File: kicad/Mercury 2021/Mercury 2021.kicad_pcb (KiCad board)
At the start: 2 copper layers, 100 x 100 mm, 46 parts, among them J1 Batt_Power, J10 3.3v rail, J13 Screw_Terminal_01x02, J14 Screw_Terminal_01x02, J15 Raspberry_Pi_2_3, J16 Sensors_Extra, J17 Arduino_Extra_Power, J18 Arduino_Extra_Comm, J19 Arduino_Extra_Digital, J2 Conn_01x20_Female, J20 Arduino_Extra_Analog, J21 MP_Extra_Analog, J3 Conn_01x20_Female, J30 Screw_Terminal_01x02, J31 Screw_Terminal_01x02, J32 Screw_Terminal_01x02, J33 Screw_Terminal_01x02, J36 GND rail 2, J37 GND rail 3, J4 Screw_Terminal_01x02, J5 Screw_Terminal_01x02, J7 5V rail, J8 GND Rail 1, J9 11v rail, U1 LM1084-5.0, U10 TCA9548APWR, U11 MDD10A, U12 PCA9685, U12C1 PCA9685, U13 MDD10A, U2 Adafruit_VL53L0X, U3 Adafruit_VL53L0X, U4 Adafruit_VL53L0X, U5 Adafruit_VL53L0X, U6 Adafruit_VL53L0X, U7 Adafruit_VL53L0X, U8 Adafruit_VL53L0X, U9 Adafruit_VL53L0X

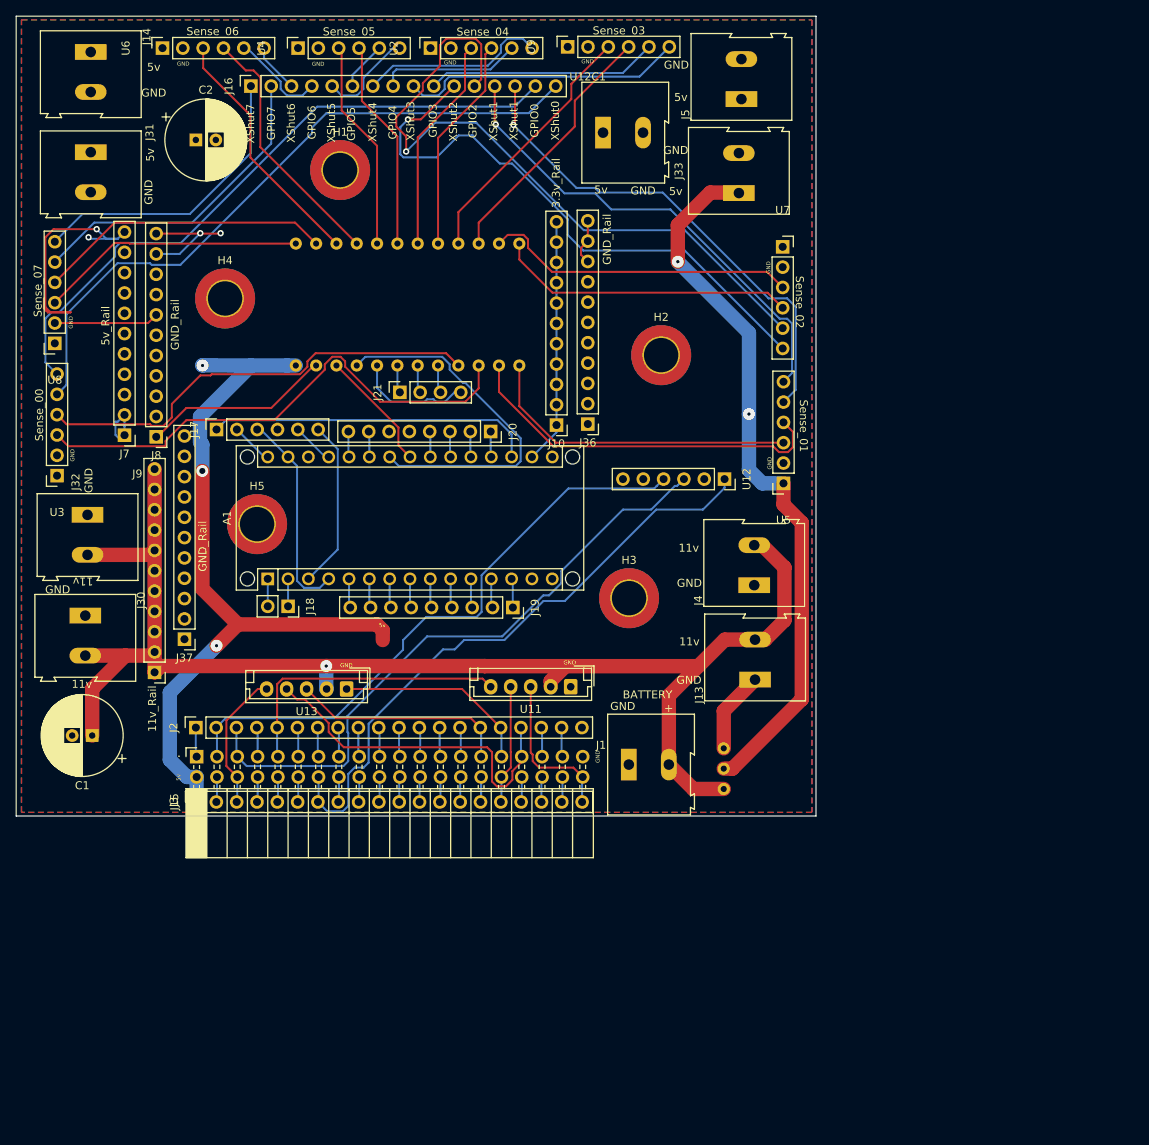
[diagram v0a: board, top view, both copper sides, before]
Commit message: NOTE! Updated PCB
This is different than the PCBs that were ordered.
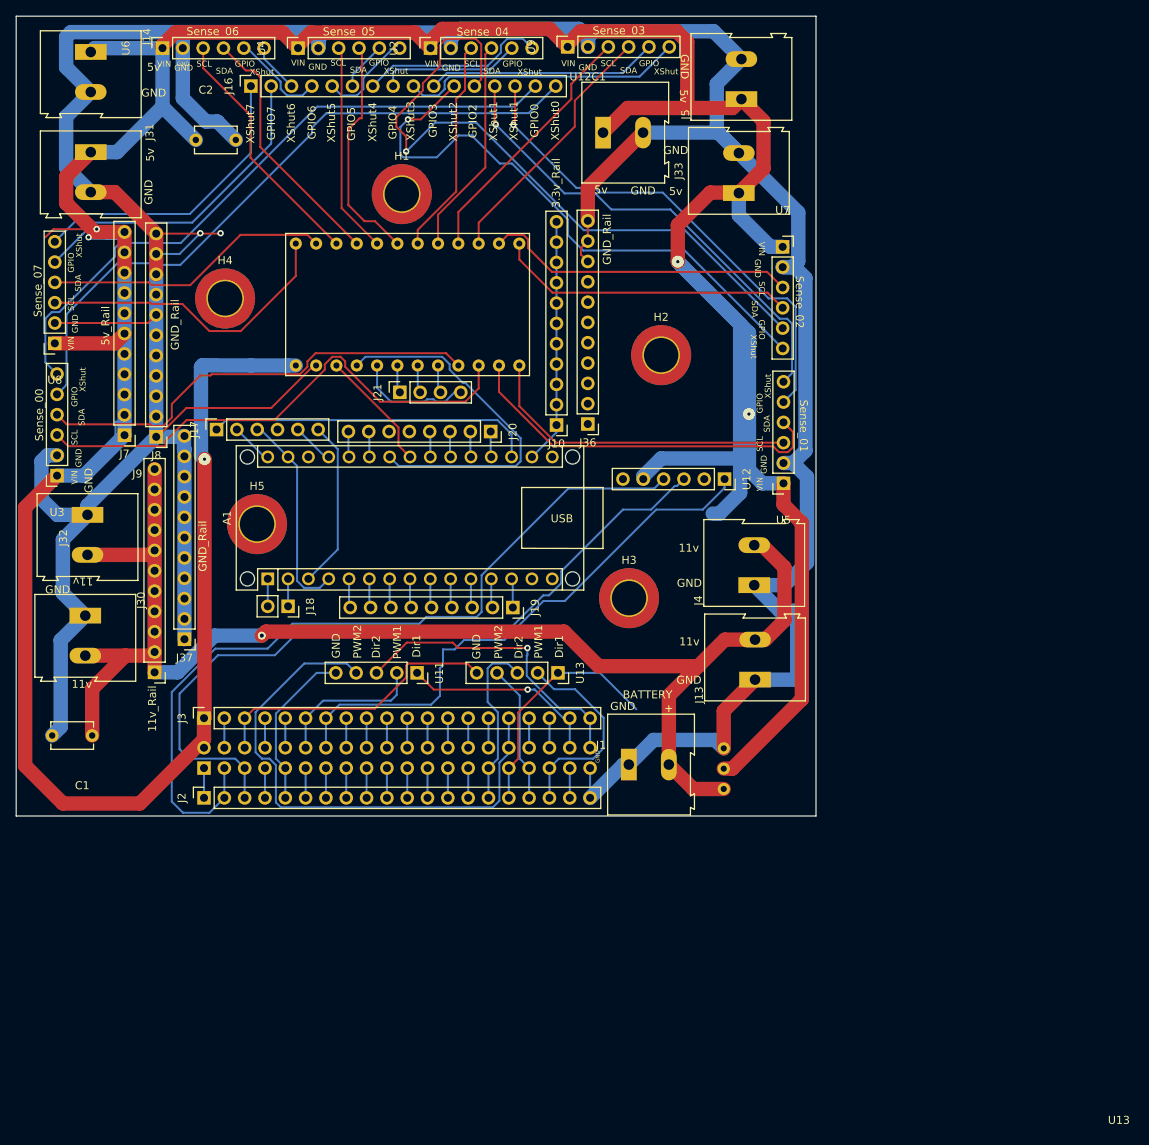
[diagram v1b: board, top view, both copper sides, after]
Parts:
- added ?: , , F.Cu at (88.8, 100.6)
- C1, C2: footprint Capacitor_THT:CP_Radial_D10.0mm_P2.50mm -> Capacitor_THT:C_Disc_D5.1mm_W3.2mm_P5.00mm
- J15: footprint Connector_PinSocket_2.54mm:PinSocket_2x20_P2.54mm_Horizontal -> Connector_PinSocket_2.54mm:PinSocket_2x20_P2.54mm_Vertical; moved to B.Cu
- U11, U13: footprint Connector_JST:JST_EH_B5B-EH-A_1x05_P2.50mm_Vertical -> Connector_PinSocket_2.54mm:PinSocket_1x05_P2.54mm_Vertical
- moved U13 26.5 mm to (85.9, 101.7), turned to 270 degrees
- moved U11 19.3 mm to (68.2, 101.7), turned to 270 degrees
- moved J3 10.5 mm to (41.6, 107.4)
- moved J2 8.84 mm to (41.6, 117.3)
- moved H1 8.28 mm to (66.3, 41.8)
- moved J15 1.70 mm to (41.6, 113.6), turned to 270 degrees
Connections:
- U11 pad 1: GND_Rail -> /Motors/Pi38
- U11 pad 2: 11.1v_Rail -> /Motors/Pi12
- U13 pad 2: 11.1v_Rail -> /Motors/LM_PWM1_GPIO19
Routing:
- net GND_Rail: track 67.4 -> 479.9 mm
- net 5v_Rail: track 224.3 -> 509.9 mm, vias 7 -> 5
- net /Motors/Pi32: track 14.9 -> 67.8 mm
- net /Motors/LM_PWM2_GPIO13: track 43.5 -> 17.3 mm
- net /Motors/Pi03: track 75.9 -> 100.5 mm
- net /Motors/LM_PWM1_GPIO19: track 3.67 -> 25.9 mm
- net /Motors/Pi38: track 3.16 -> 25.2 mm, vias 0 -> 1
- net /Motors/LM_GND: track 17.4 -> 36.9 mm
- net /Motors/Pi40: track 19.6 -> 38.0 mm, vias 0 -> 1
- net /Motors/Pi09: track 36.5 -> 20.6 mm
- net /Motors/Pi12: track 3.16 -> 19.0 mm
- net /Motors/Pi05: track 79.2 -> 94.8 mm
- net /Motors/Pi14: track 77.5 -> 69.8 mm
- net /Motors/LM_DIR2_GPIO5: track 27.4 -> 21.7 mm
- net /Sensors/SCL7: track 33.3 -> 38.5 mm
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- removed copper zone on F.Cu, net 5v_Rail
- removed copper zone on B.Cu, net GND_Rail
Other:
- board text added: "Dir1"
- board text added: "Dir2"
- board text added: "GPIO"
- board text added: "PWM1"
- board text added: "PWM2"
- board text added: "SCL"
- board text added: "SDA"
- board text added: "USB"
- board text added: "VIN"
- board text added: "XShut"
- board text removed: "•"

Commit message: Updated PCB
Updated Labels & arduino now powered off of board.
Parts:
- moved J2 0.12 mm to (41.6, 117.2)
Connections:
- A1 pad 29: /Sensors/Arduino_GND -> GND_Rail
- A1 pad 30: /Sensors/Arduino_VIN -> 5v_Rail
- A1 pad 4: /Sensors/Arduino_GND -> GND_Rail
- J17 pad 2: /Sensors/Arduino_VIN -> 5v_Rail
- J17 pad 3: /Sensors/Arduino_GND -> GND_Rail
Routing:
- net GND_Rail: track 479.9 -> 523.6 mm
- net /Sensors/Arduino_GND: track 26.0 -> 0.00 mm
- net 5v_Rail: track 509.9 -> 524.9 mm
- net /Sensors/Arduino_VIN: track 5.28 -> 0.00 mm
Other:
- board text added: "01"
- board text added: "05"
- board text added: "06"
- board text added: "09"
- board text added: "12"
- board text added: "13"
- board text added: "18"
- board text added: "19"
- board text added: "20"
- board text added: "21"
- board text added: "29"
- board text added: "31"
- board text added: "32"
- board text added: "33"
- board text added: "35"
- board text added: "38"
- board text added: "40"
- board text added: "AREF"
- board text added: "Board by: MaxMyzer With contributions from: c3n3"
- board text added: "NC"
- board text added: "Pi GPIO"
- board text added: "Pi Pin"
- board text added: "reset"
- board text removed: "Board by: Max Myzer With contributions from: c3n3"

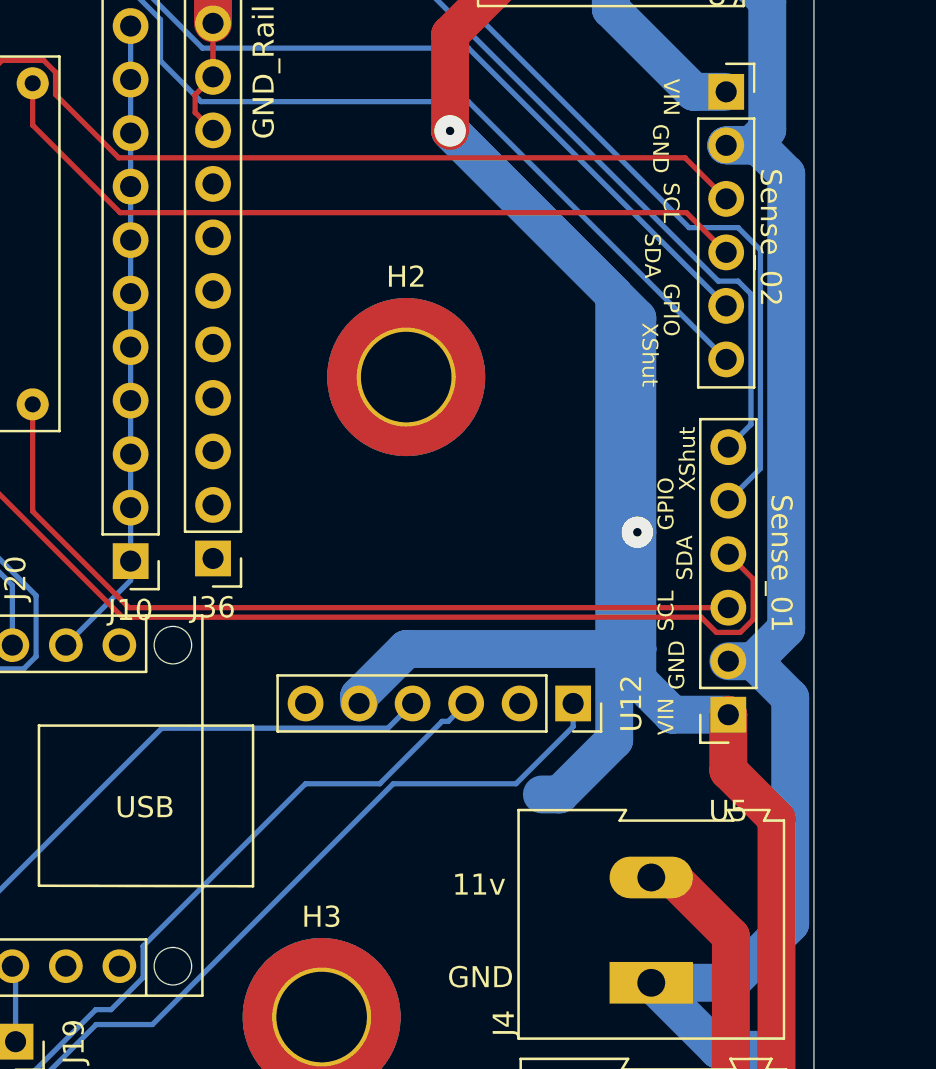
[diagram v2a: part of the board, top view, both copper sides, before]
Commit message: Updated PCB
Flipped connector around
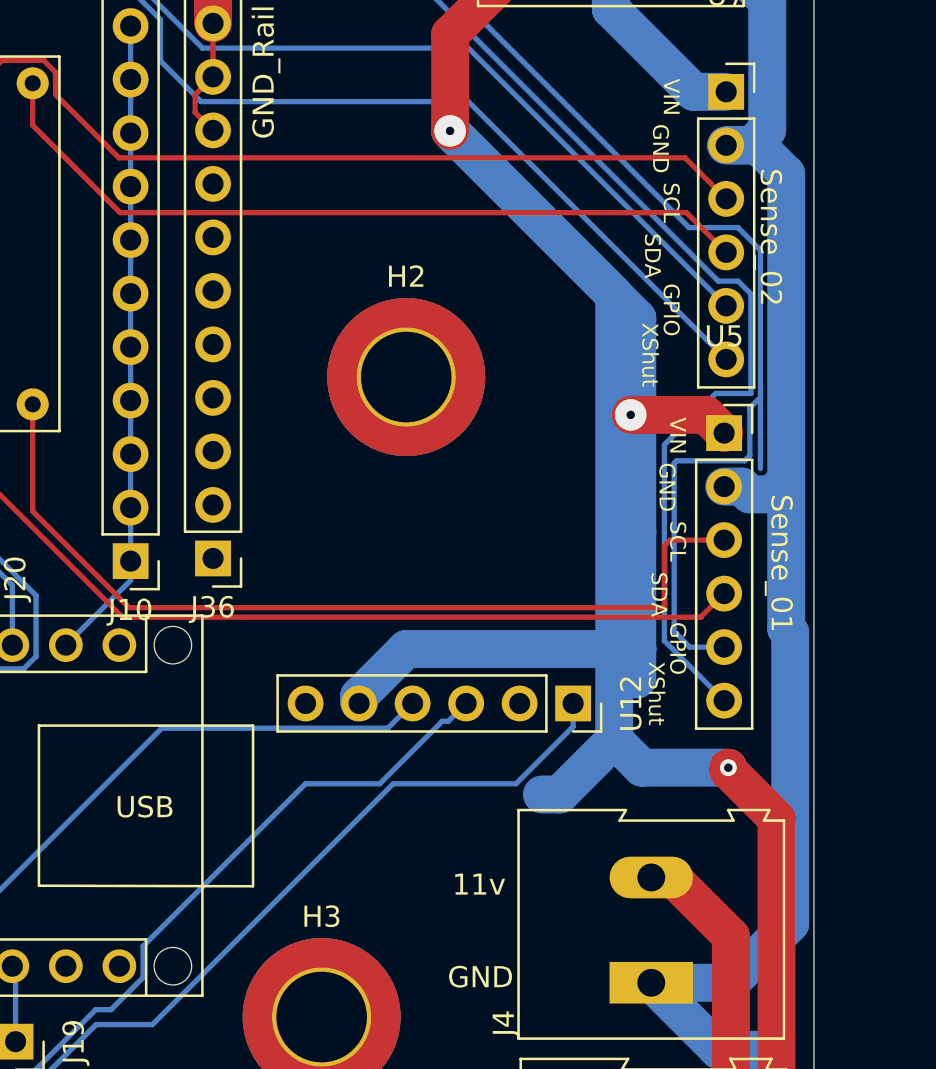
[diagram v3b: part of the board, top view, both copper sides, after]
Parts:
- moved U5 23.5 mm to (113.8, 59.6), turned to 0 degrees
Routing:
- net /Sensors/Sense1_XShut: track 60.0 -> 75.4 mm
- net /Sensors/Sense1_GPIO: track 62.4 -> 77.6 mm
- net /Sensors/SDA1: track 47.0 -> 42.0 mm
- net 5v_Rail: track 524.9 -> 528.1 mm, vias 5 -> 6
- net /Sensors/SCL1: track 40.0 -> 42.9 mm
- net GND_Rail: track 523.6 -> 524.5 mm
